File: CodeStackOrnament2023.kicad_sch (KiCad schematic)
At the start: 26 parts, among them SW1 SW_SPST, U1 TLC555xD, U2 74VHC4040FT

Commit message: more routing
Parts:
- U2: footprint Package_SO:TSSOP-16_4.4x5mm_P0.65mm -> CodeStackOrnament2023Footprints:CD74HC4040M96_SOIC16
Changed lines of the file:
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@@
       (effects (font (size 1.27 1.27)) (justify left))
     )
-    (property "Footprint" "Package_SO:TSSOP-16_4.4x5mm_P0.65mm" (at 140.97 64.77 0)
+    (property "Footprint" "CodeStackOrnament2023Footprints:CD74HC4040M96_SOIC16" (at 140.97 64.77 0)
       (effects (font (size 1.27 1.27)) hide)
     )

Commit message: adding gerbers
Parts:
- C3: value 1uF -> 10uF
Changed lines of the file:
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@@
       (effects (font (size 1.27 1.27)) (justify left))
     )
-    (property "Value" "1uF" (at 87.249 93.376 0)
+    (property "Value" "10uF" (at 87.249 93.376 0)
       (effects (font (size 1.27 1.27)) (justify left))
     )

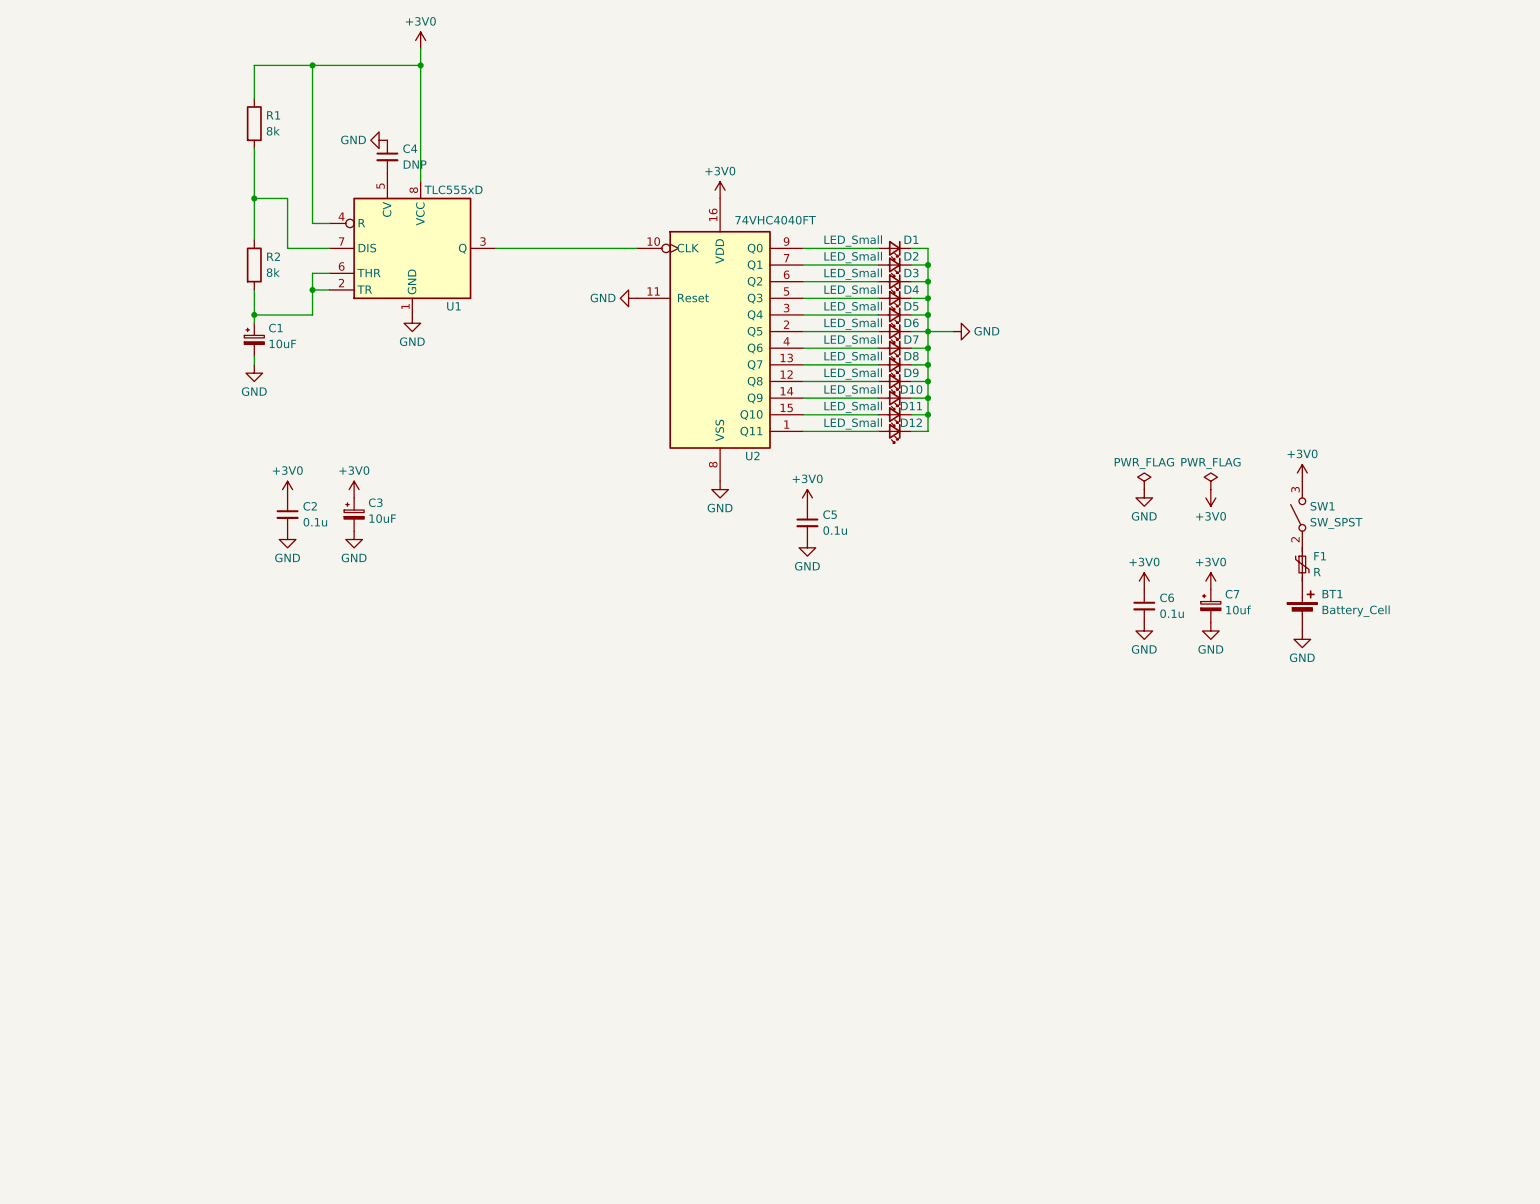
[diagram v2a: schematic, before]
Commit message: adding gerbers. cleaning up schematic.
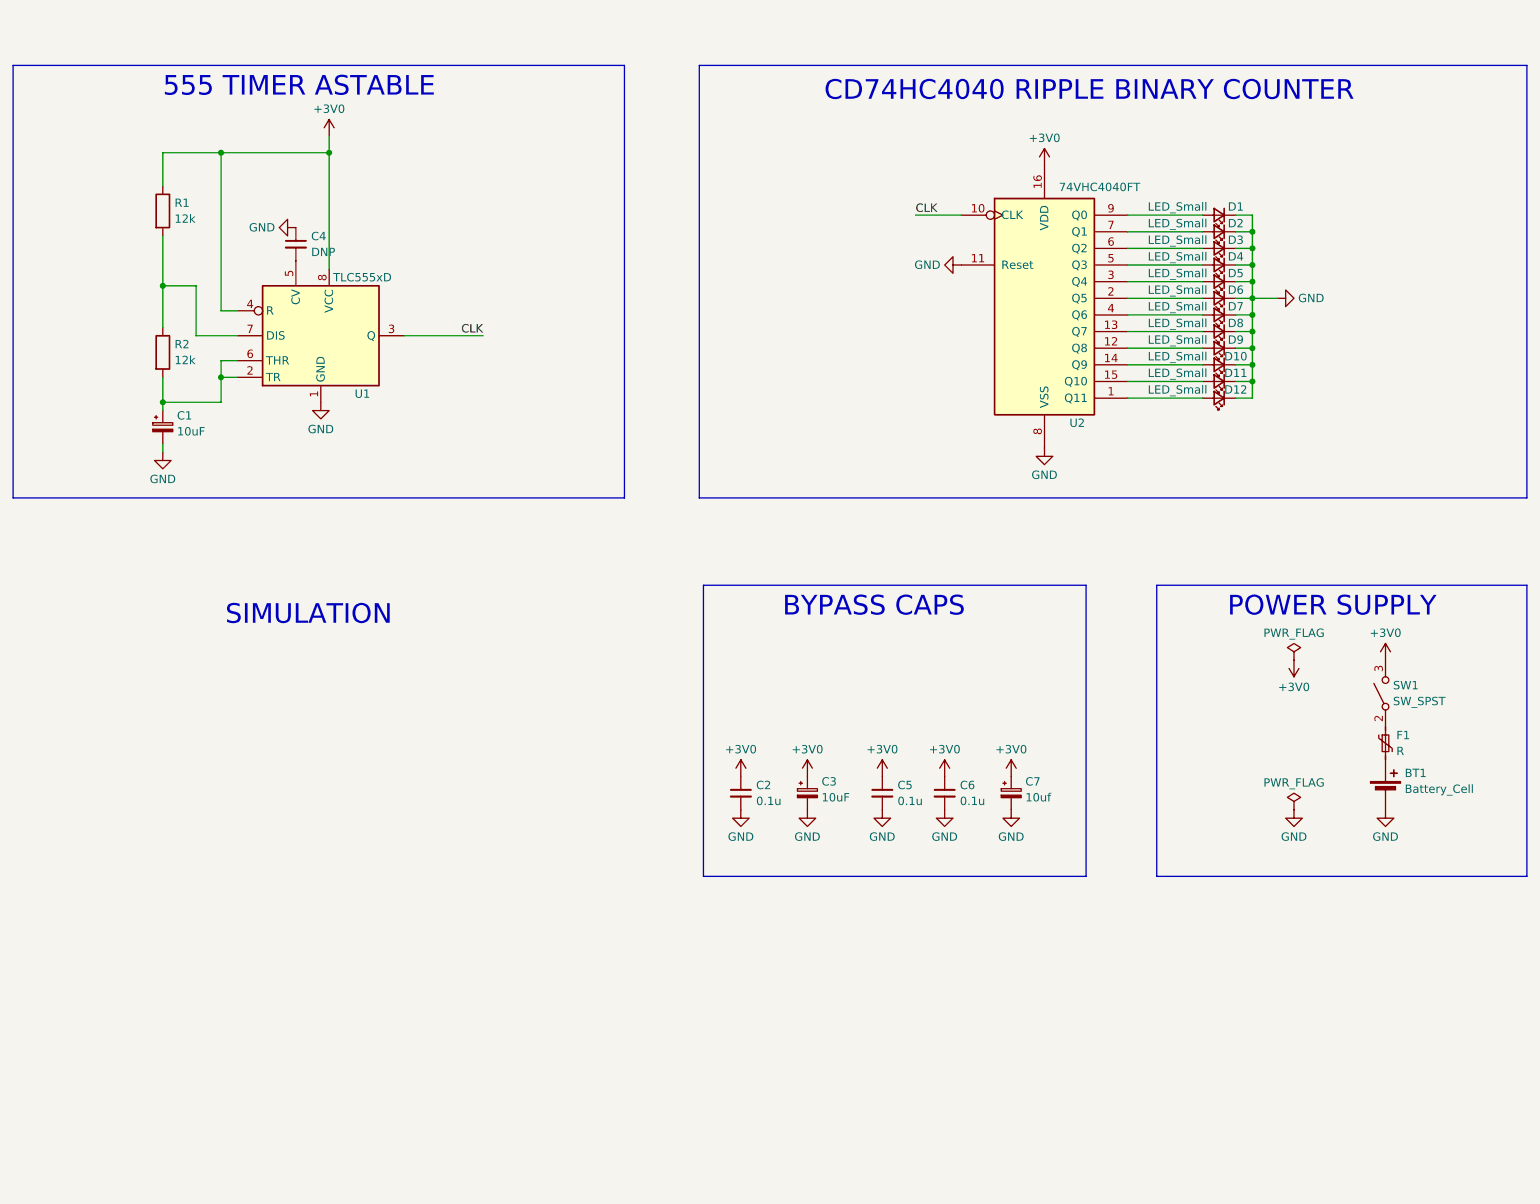
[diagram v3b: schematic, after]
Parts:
- R1, R2: value 8k -> 12k
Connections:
- net CLK: now reaches U1.3 (Q), U2.10 (CLK)
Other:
- note added: "555 TIMER ASTABLE"
- note added: "BYPASS CAPS"
- note added: "CD74HC4040 RIPPLE BINARY COUNTER"
- note added: "POWER SUPPLY"
- note added: "SIMULATION"
- title: (none) -> CodeStack Team C 2023 Ornament
- moved on the sheet: BT1, C1, C2, C3, C4, C5, C6, C7, D1, D10, D11, D12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

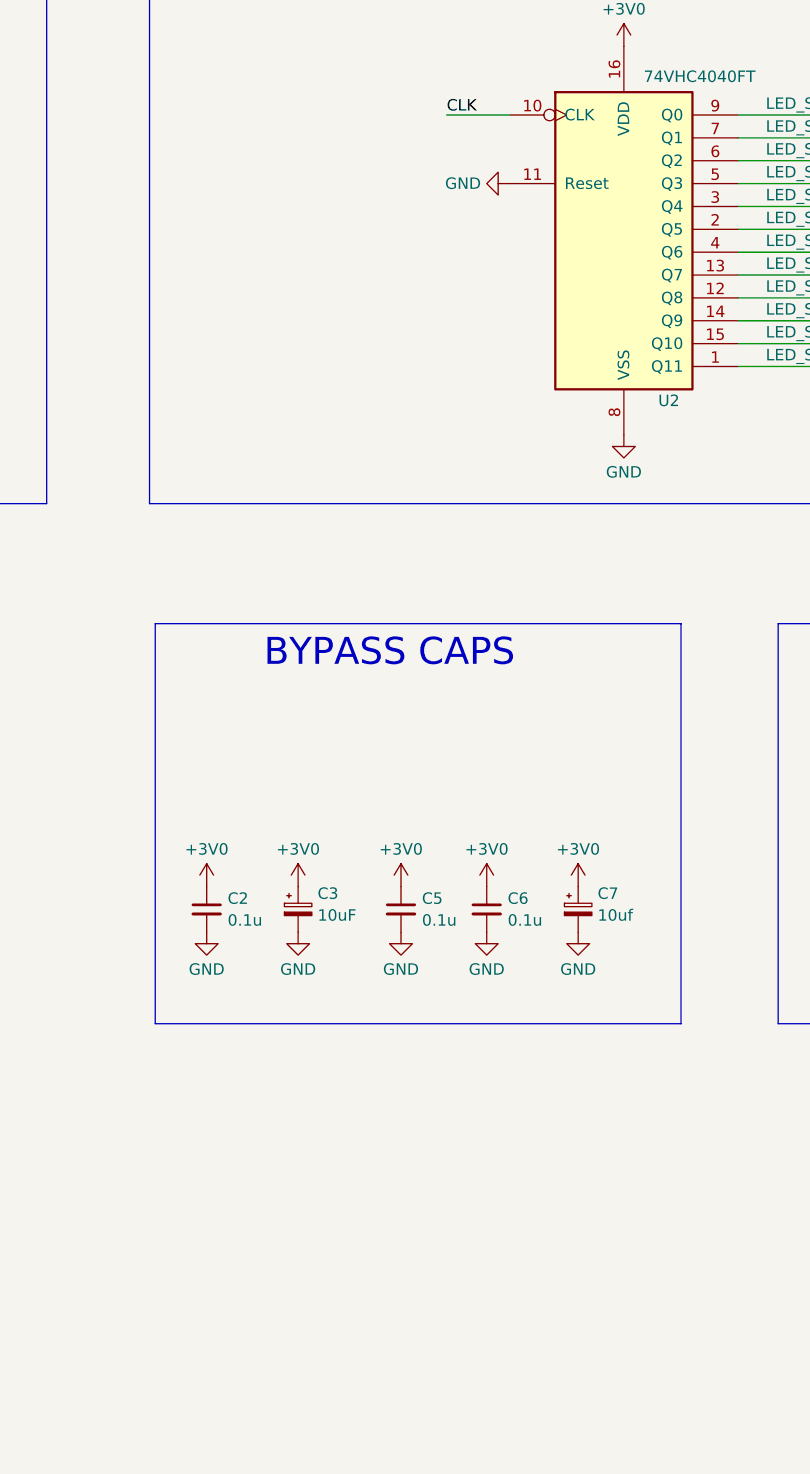
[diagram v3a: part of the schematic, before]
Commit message: starting rev 1.b with added reset circuitry.
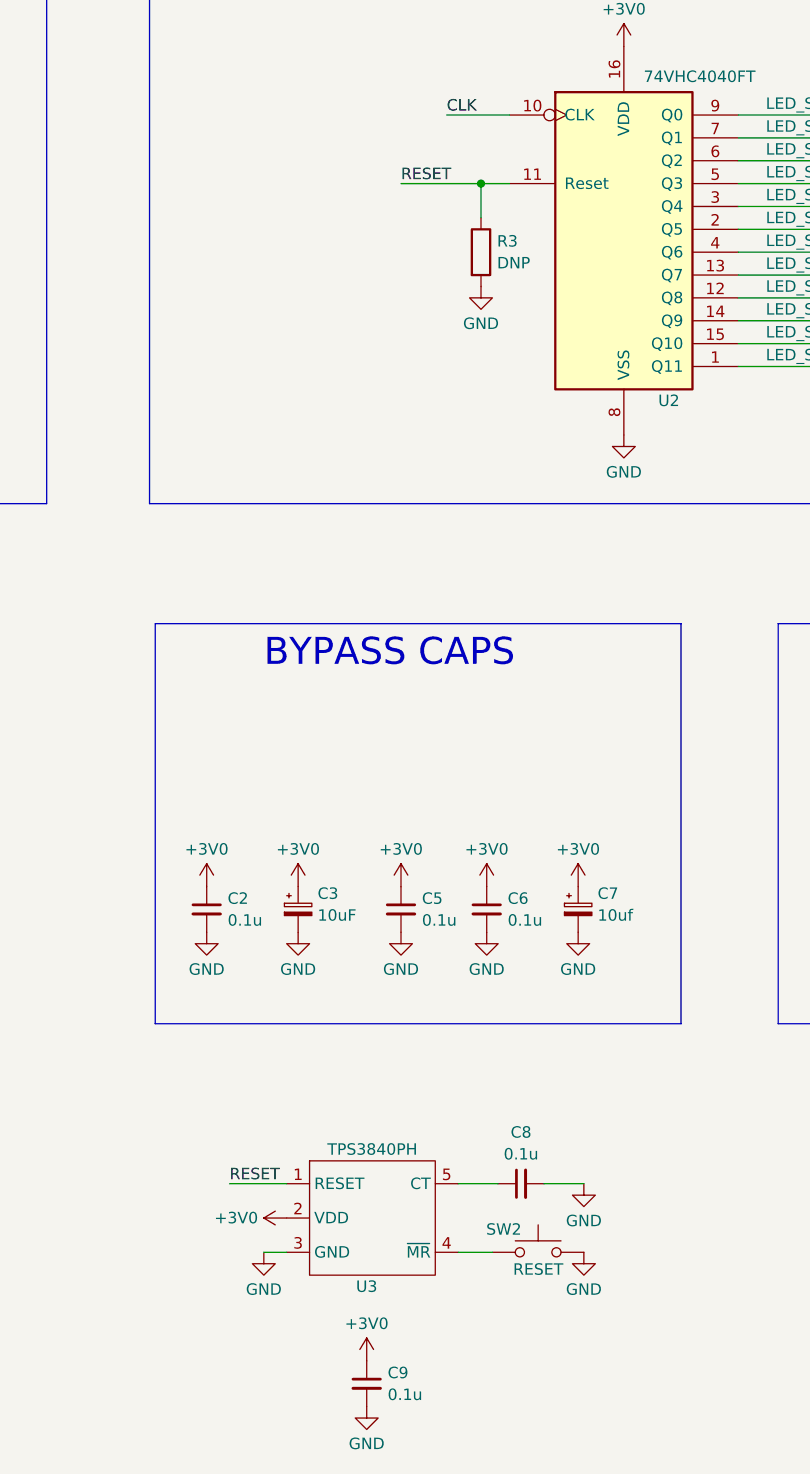
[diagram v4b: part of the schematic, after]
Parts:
- added C8, C9: 0.1u, Capacitor_SMD:C_0805_2012Metric, symbol Device:C_Small
- added R3: DNP, Resistor_SMD:R_0805_2012Metric, symbol Device:R
- added SW2: RESET, symbol Switch:SW_Push
- added U3: TPS3840PH, symbol CodeStackOrnament2023Library:TPS3840PH
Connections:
- net +3V0: now also C9.1, U3.2 (VDD)
- net GND: now also C8.2, C9.2, R3.2, SW2.2, U3.3 (GND); no longer U2.11 (Reset)
- new net: SW2.1, U3.4 (~{MR})
- new net: C8.1, U3.5 (CT)
- new net RESET: R3.1, U2.11 (Reset), U3.1 (RESET)

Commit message: rev 1.b adding footprints
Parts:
- U3: footprint (none) -> CodeStackOrnament2023Footprints:TPS3840_RESET
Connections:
- net GND: now also SW2.4; no longer SW2.2
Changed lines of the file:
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@@
       (effects (font (size 1.27 1.27)))
     )
-    (property "Footprint" "" (at 160.655 170.815 0)
+    (property "Footprint" "CodeStackOrnament2023Footprints:TPS3840_RESET" (at 160.655 170.815 0)
       (effects (font (size 1.27 1.27)) hide)
     )
@@
     )
     (pin "1")
-    (pin "2")
-    (instances
-      (project "CodeStackOrnament2023"
+    (pin "4")
+    (instances
+      (project "CodeStackOrnament2023"

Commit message: finshed routing rev 1.b with reset circuit
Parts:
- SW2: footprint (none) -> CodeStackOrnament2023Footprints:PTS815_SWITCH
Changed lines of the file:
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@@
       (effects (font (size 1.27 1.27)))
     )
-    (property "Footprint" "" (at 180.975 168.275 0)
+    (property "Footprint" "CodeStackOrnament2023Footprints:PTS815_SWITCH" (at 180.975 168.275 0)
       (effects (font (size 1.27 1.27)) hide)
     )

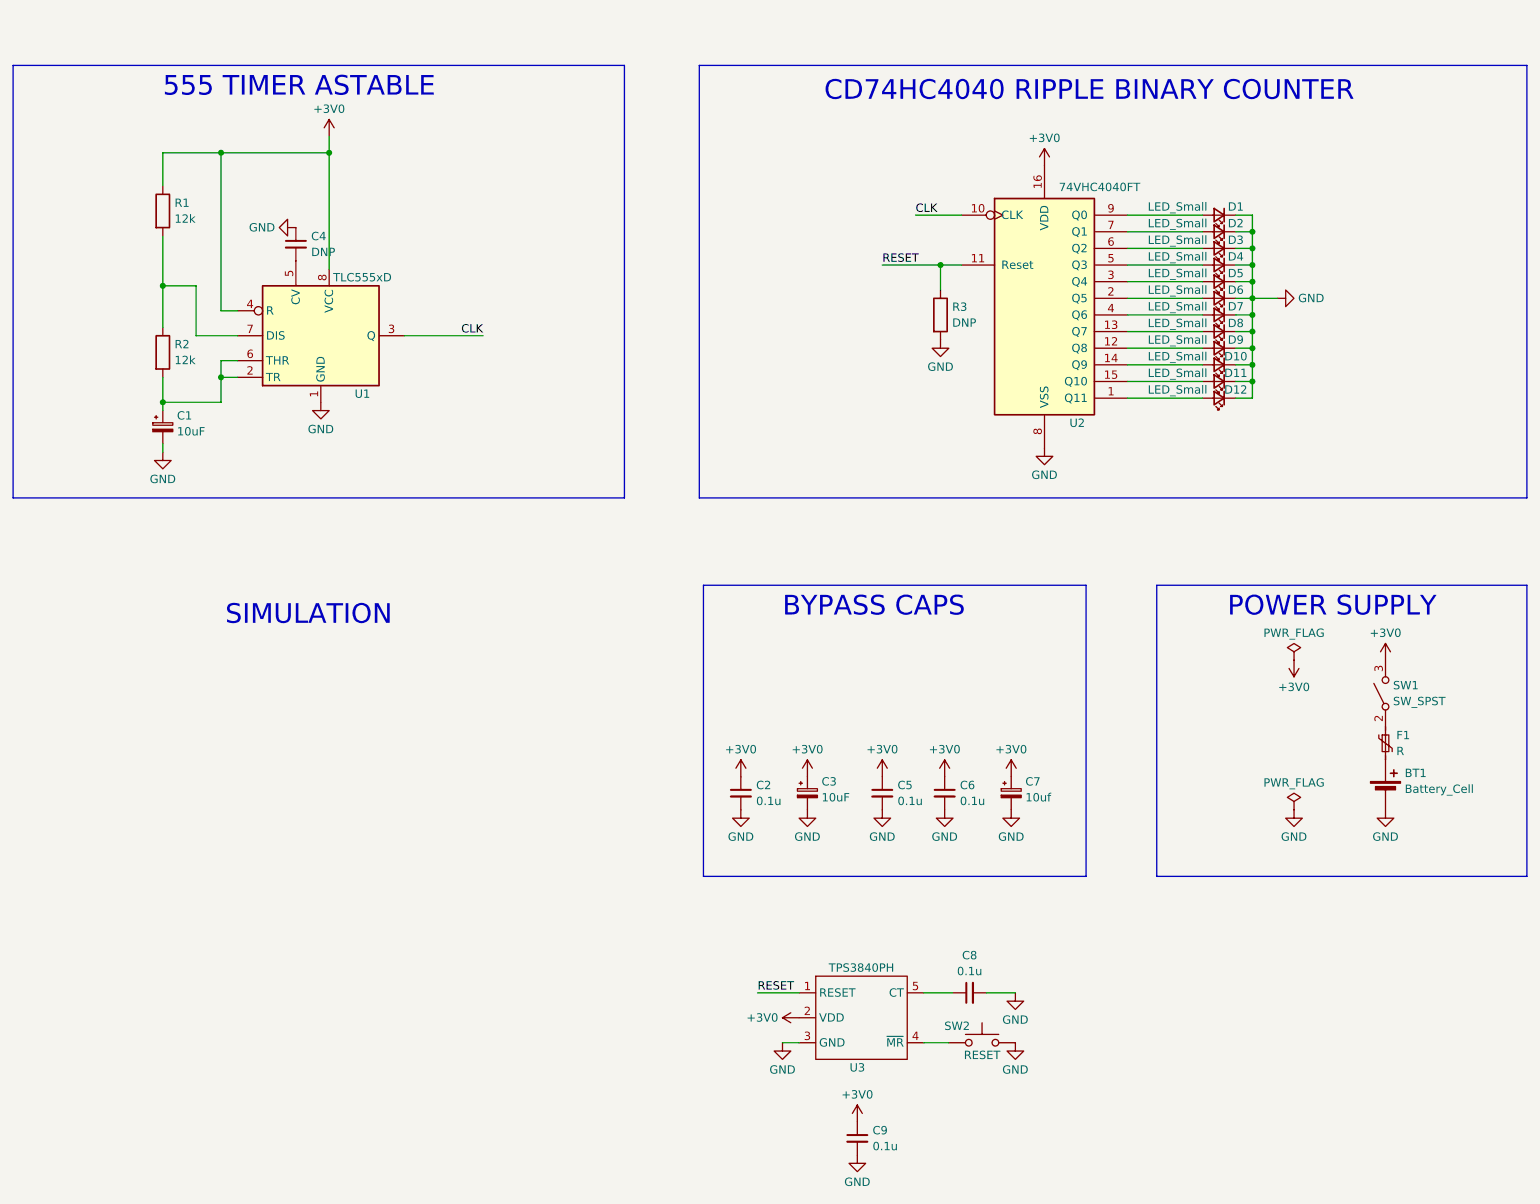
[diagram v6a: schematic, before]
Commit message: rev 1.b added a reset circuit to ensure counter starts at 0. Reorganizing schematic.
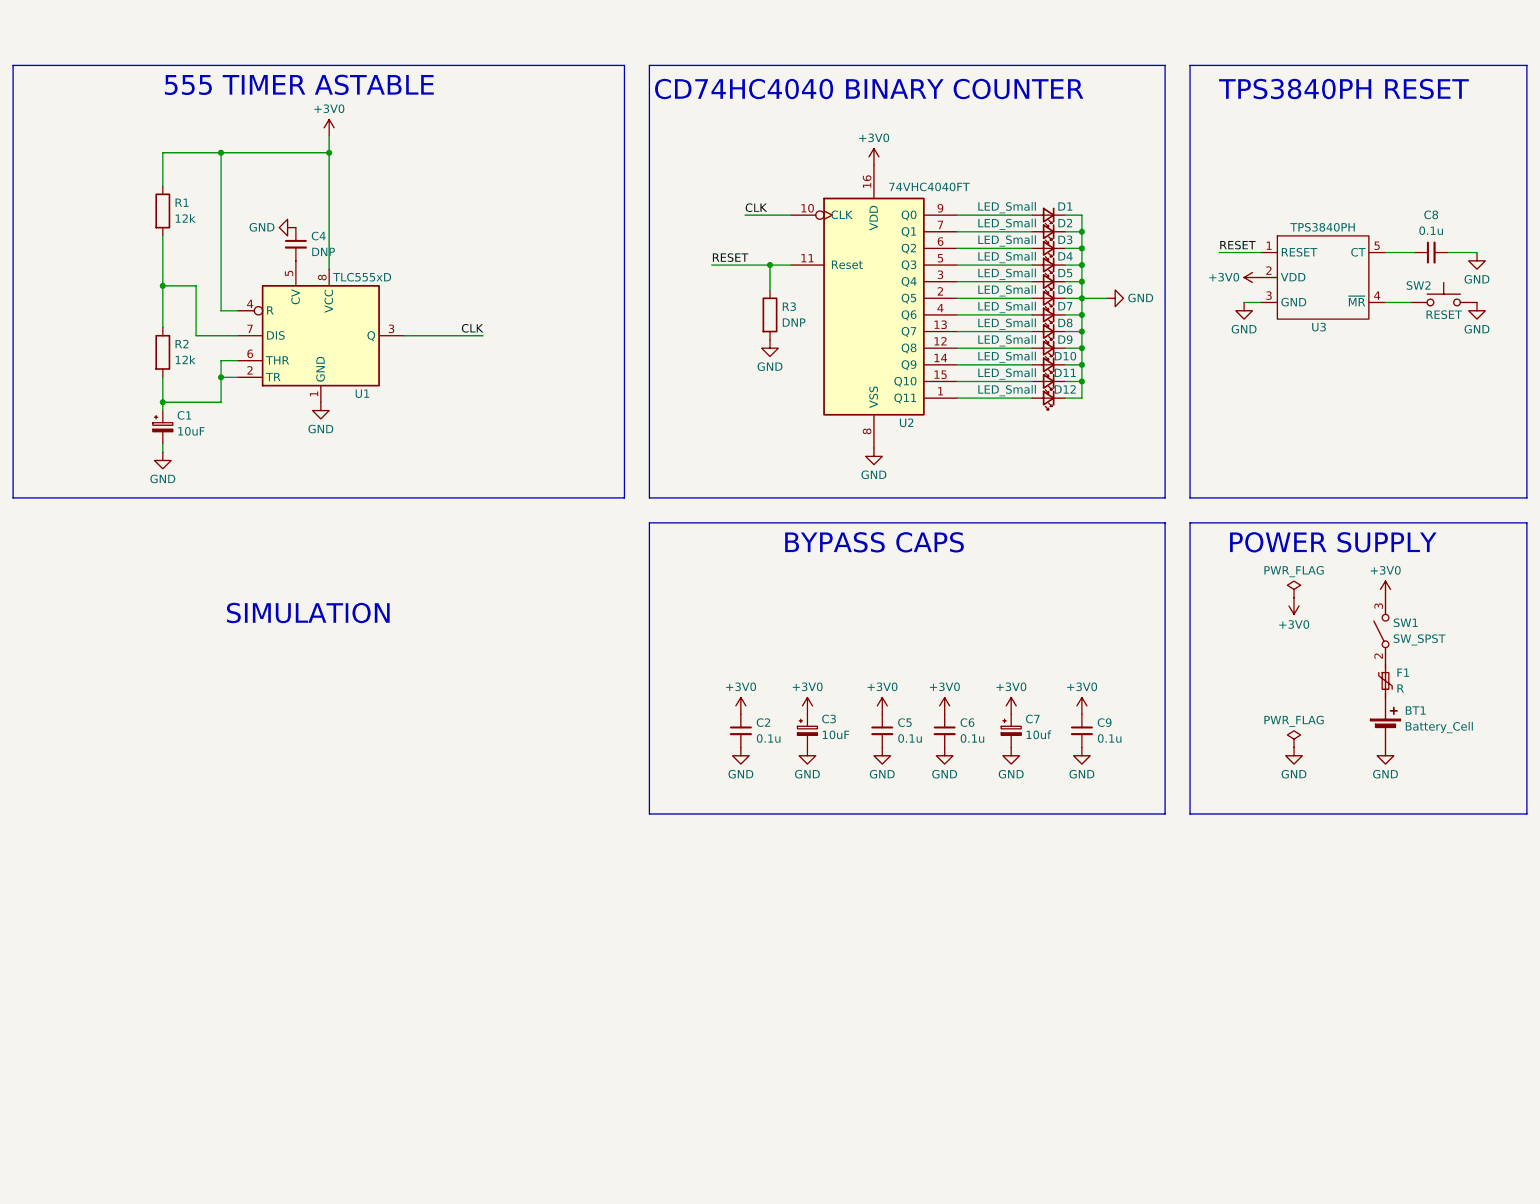
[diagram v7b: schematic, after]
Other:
- note added: "CD74HC4040 BINARY COUNTER"
- note added: "TPS3840PH RESET"
- note removed: "CD74HC4040 RIPPLE BINARY COUNTER"
- moved on the sheet: BT1, C2, C3, C5, C6, C7, C8, C9, D1, D10, D11, D12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
